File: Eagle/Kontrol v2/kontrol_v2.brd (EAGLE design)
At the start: 84.3 x 132.8 mm, 34 parts, among them K1 SRD-12VDC-SL-C

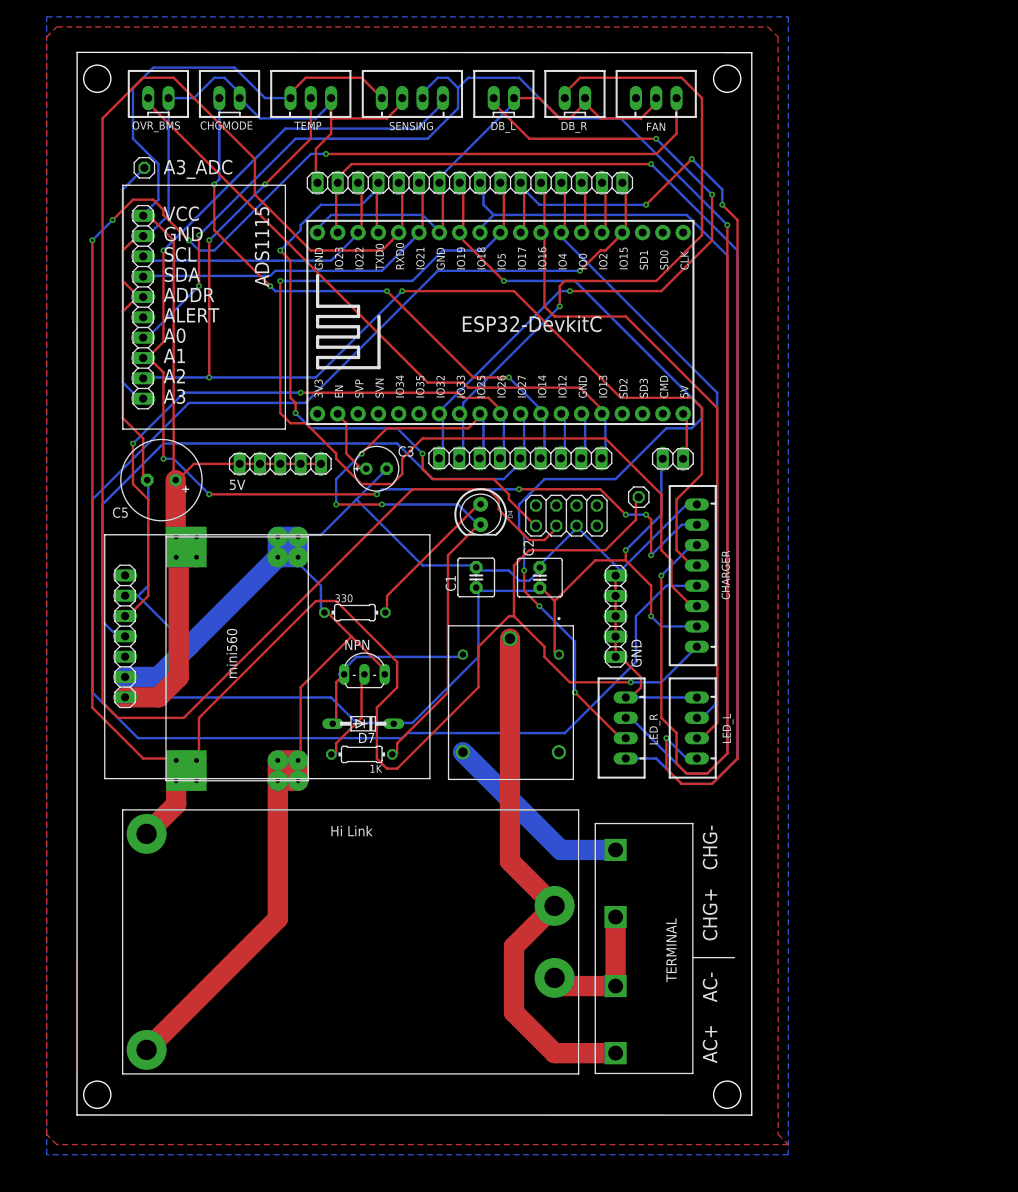
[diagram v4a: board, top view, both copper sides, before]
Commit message: Update kontrol
XH8 -> xh10
4p term -> 2p term x2
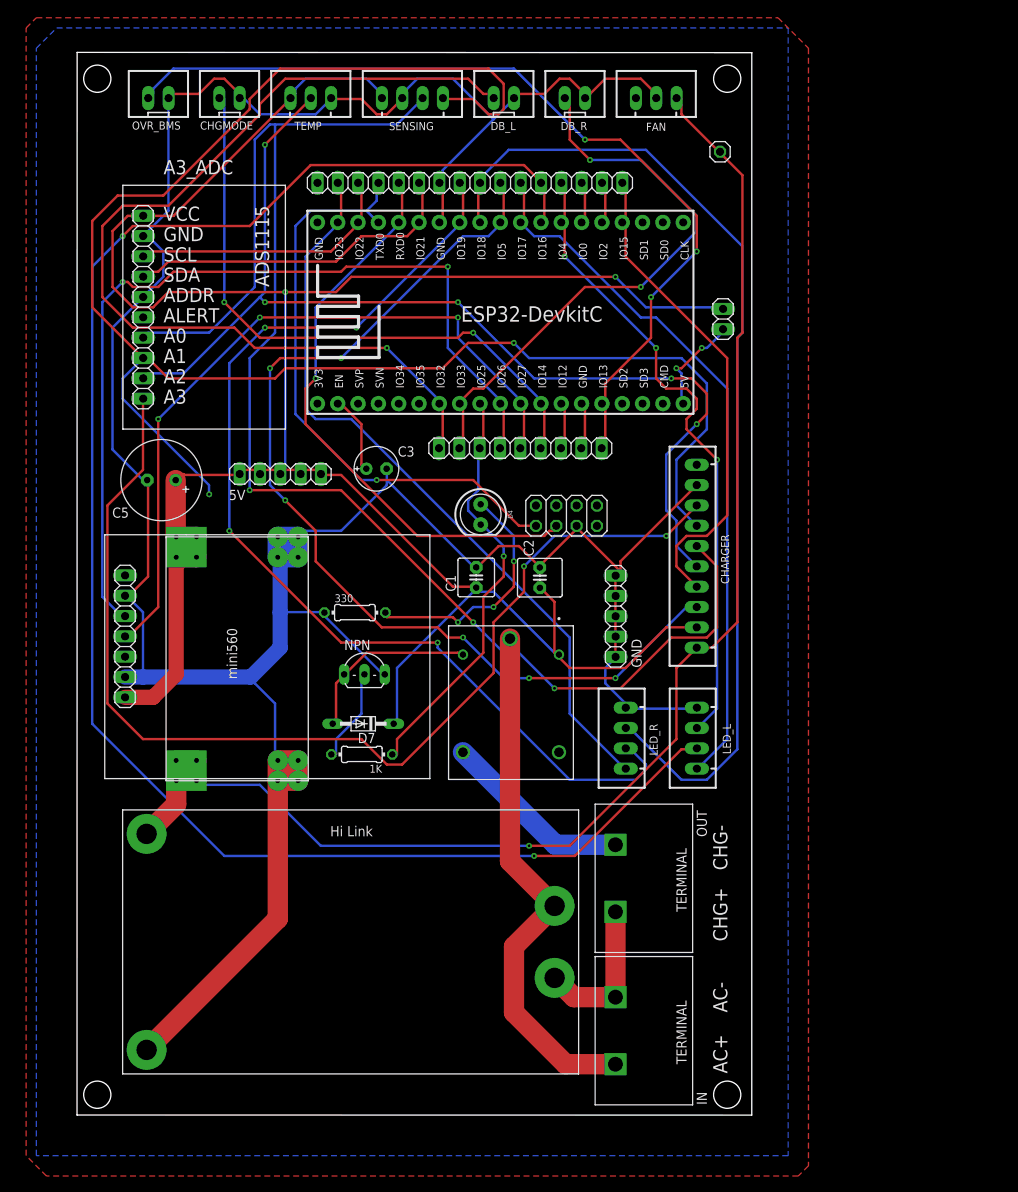
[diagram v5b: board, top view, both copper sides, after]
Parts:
- removed JP8: (no value), pinhead:1X01
- removed U$4: TERMINAL_4P, TA_library:TERMINAL_4P
- added IN, OUT: TERMINAL_2P, TA_library:TERMINAL_2P
- CHARGER: value JST-XH-08-PIN-LONG-PAD -> JST-XH-10-PIN-LONG-PAD; device Rembrandt Electronics - JST XH Connectors v1-0:JST-XH-08-PACKAGE-LONG-PAD -> Rembrandt Electronics - JST XH Connectors v1-0:JST-XH-10-PACKAGE-LONG-PAD
- moved JP4 44.4 mm to (80.4, 120.4)
- moved JP7 18.6 mm to (80.8, 99.5), turned to 270 degrees
- moved CHARGER 2.42 mm to (77.5, 69.8)
- moved U$1 1.27 mm to (52.9, 100.3)
- moved 5V 1.27 mm to (25.4, 80.1)
- moved JP6 1.27 mm to (55.4, 83.4)
- moved LED_L 1.27 mm to (77.5, 47.1)
- moved LED_R 1.27 mm to (68.6, 47.1)
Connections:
- removed net N$44: JP8.1, U$2.A3
- new net HV_SENSE: CHARGER.8, U$2.A3
- new net N$14: CHARGER.10
- net AC+: now also IN.2, OUT.1; no longer U$4.P$2, U$4.P$3
- net AC-: now also IN.1; no longer U$4.P$1
- net AC_OUT_CHG: now also OUT.2; no longer U$4.P$4
- net GND: now also CHARGER.9; no longer CHARGER.8
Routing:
- net PWM_DISCHARGE: track 200.1 -> 61.6 mm, vias 1 -> 0
- net 12V: track 315.3 -> 177.6 mm, vias 5 -> 1
- net HV_SENSE: track 0.00 -> 135.8 mm, vias 0 -> 2
- net TX_BMS: track 205.0 -> 73.3 mm, vias 0 -> 1
- net RED_KIRI: track 85.7 -> 212.9 mm, vias 0 -> 2
- net VOLTAGE_SENSE: track 148.6 -> 211.2 mm, vias 8 -> 2
- net GRN_KANAN: track 142.4 -> 94.9 mm, vias 1 -> 0
- net 5V: track 264.2 -> 307.1 mm
- net GRN_KIRI: track 129.0 -> 89.0 mm, vias 4 -> 0
- net DETEKSI_BATERAI_KIRI: track 87.7 -> 121.4 mm, vias 3 -> 1
- net OVERRIDE_BMS: track 80.2 -> 112.6 mm, vias 0 -> 3
- net RX_IOT: track 80.3 -> 112.2 mm
- net N$44: track 31.4 -> 0.00 mm
- net RELAY: track 83.4 -> 53.0 mm, vias 3 -> 1
- net RED_KANAN: track 110.2 -> 132.4 mm
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
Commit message: update kontrol
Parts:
- renumbered 330 to R2
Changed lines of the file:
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@@
 <drawing>
 <settings>
-<setting alwaysvectorfont="yes"/>
+<setting alwaysvectorfont="no"/>
 <setting verticaltext="up"/>
 </settings>
@@
 <attribute name="VALUE" x="47.074109375" y="75.04679375" size="0.6096" layer="27" font="vector" ratio="20" rot="R270" align="top-center"/>
 </element>
-<element name="330" library="rcl" library_urn="urn:adsk.eagle:library:334" package="0204/7" package3d_urn="urn:adsk.eagle:package:23498/2" value="6k" x="34.742409375" y="62.80399375" smashed="yes">
+<element name="R2" library="rcl" library_urn="urn:adsk.eagle:library:334" package="0204/7" package3d_urn="urn:adsk.eagle:package:23498/2" value="6k" x="34.742409375" y="62.80399375" smashed="yes">
 <attribute name="NAME" x="32.202409375" y="64.09939375" size="0.9906" layer="25" ratio="10"/>
 <attribute name="POPULARITY" value="48" x="34.742409375" y="62.80399375" size="1.778" layer="27" display="off"/>
@@
 <contactref element="U$3" pad="GND1"/>
 <contactref element="U$3" pad="GND"/>
-<contactref element="330" pad="1"/>
+<contactref element="R2" pad="1"/>
 <contactref element="GND" pad="1"/>
 <contactref element="GND" pad="2"/>
@@
 <signal name="N$1">
 <contactref element="D4" pad="A"/>
-<contactref element="330" pad="2"/>
+<contactref element="R2" pad="2"/>
 <wire x1="46.99" y1="62.23" x2="38.735" y2="62.23" width="0.3048" layer="1"/>
 <wire x1="47.625" y1="61.595" x2="46.99" y2="62.23" width="0.3048" layer="1"/>

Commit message: update kontrol
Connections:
- net N$1: now also D4.K; no longer D4.A
- net RELAY: now also D4.A; no longer D4.K
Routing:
- net N$1: track 30.7 -> 82.6 mm
- net RELAY: track 53.0 -> 52.0 mm
- net GND: track 396.7 -> 397.7 mm
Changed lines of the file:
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@@
 <wire x1="8.255" y1="54.75219375" x2="8.255" y2="62.865" width="0.3048" layer="16"/>
 <wire x1="6.35" y1="64.77" x2="6.015009375" y2="64.91219375" width="0.3048" layer="16"/>
-<wire x1="38.735" y1="78.74" x2="38.735" y2="79.375" width="0.3048" layer="16"/>
-<wire x1="38.735" y1="79.375" x2="38.735" y2="80.645" width="0.3048" layer="16"/>
-<wire x1="33.02" y1="73.025" x2="38.735" y2="78.74" width="0.3048" layer="16"/>
-<wire x1="28.575" y1="73.025" x2="33.02" y2="73.025" width="0.3048" layer="16"/>
+<wire x1="38.735" y1="76.2" x2="38.735" y2="78.105" width="0.3048" layer="16"/>
+<wire x1="38.735" y1="78.105" x2="38.735" y2="80.645" width="0.3048" layer="16"/>
+<wire x1="35.56" y1="73.025" x2="38.735" y2="76.2" width="0.3048" layer="16"/>
+<wire x1="28.575" y1="73.025" x2="35.56" y2="73.025" width="0.3048" layer="16"/>
 <wire x1="38.735" y1="80.645" x2="38.704809375" y2="80.78719375" width="0.3048" layer="16"/>
 <wire x1="28.575" y1="73.025" x2="27.644409375" y2="72.26419375" width="0.3048" layer="16"/>
@@
 <wire x1="25.4" y1="62.865" x2="30.48" y2="62.865" width="0.3048" layer="16"/>
 <wire x1="30.48" y1="62.865" x2="30.932409375" y2="62.80399375" width="0.3048" layer="16"/>
-<wire x1="38.735" y1="79.375" x2="49.53" y2="68.58" width="0.3048" layer="16"/>
-<wire x1="49.53" y1="68.58" x2="49.905409375" y2="68.46619375" width="0.3048" layer="16"/>
+<wire x1="38.735" y1="78.105" x2="48.37380625" y2="68.46619375" width="0.3048" layer="16"/>
+<wire x1="48.37380625" y1="68.46619375" x2="49.905409375" y2="68.46619375" width="0.3048" layer="16"/>
 <wire x1="24.765" y1="51.435" x2="24.765" y2="44.45" width="0.3048" layer="16"/>
 <wire x1="22.225" y1="53.975" x2="24.765" y2="51.435" width="0.3048" layer="16"/>
@@
 <contactref element="JP6" pad="7"/>
 <contactref element="U$1" pad="9"/>
-<contactref element="D4" pad="K"/>
 <wire x1="50.8" y1="88.9" x2="50.8" y2="83.82" width="0.3048" layer="1"/>
 <wire x1="50.8" y1="83.82" x2="50.338009375" y2="83.35259375" width="0.3048" layer="1"/>
@@
 <wire x1="53.34" y1="67.31" x2="50.8" y2="64.77" width="0.3048" layer="1"/>
 <wire x1="53.34" y1="69.85" x2="53.34" y2="67.31" width="0.3048" layer="1"/>
-<wire x1="53.34" y1="71.12" x2="53.34" y2="69.85" width="0.3048" layer="16"/>
-<wire x1="50.8" y1="73.66" x2="53.34" y2="71.12" width="0.3048" layer="16"/>
 <wire x1="40.005" y1="45.085" x2="39.416009375" y2="45.07479375" width="0.3048" layer="1"/>
-<wire x1="50.8" y1="73.66" x2="50.465009375" y2="73.80219375" width="0.3048" layer="16"/>
-<wire x1="50.165" y1="78.105" x2="50.165" y2="83.185" width="0.3048" layer="16"/>
-<wire x1="48.895" y1="76.835" x2="50.165" y2="78.105" width="0.3048" layer="16"/>
-<wire x1="48.895" y1="75.565" x2="48.895" y2="76.835" width="0.3048" layer="16"/>
-<wire x1="50.165" y1="74.295" x2="48.895" y2="75.565" width="0.3048" layer="16"/>
+<wire x1="50.165" y1="76.5175" x2="50.165" y2="83.185" width="0.3048" layer="16"/>
 <wire x1="50.165" y1="83.185" x2="50.338009375" y2="83.35259375" width="0.3048" layer="16"/>
-<wire x1="50.165" y1="74.295" x2="50.465009375" y2="73.80219375" width="0.3048" layer="16"/>
 <via x="53.34" y="69.85" extent="1-16" drill="0.35"/>
+<contactref element="D4" pad="A"/>
+<wire x1="50.165" y1="76.5175" x2="50.465009375" y2="76.34219375" width="0.3048" layer="16"/>
+<wire x1="53.34" y1="73.3425" x2="50.4825" y2="76.2" width="0.3048" layer="16"/>
+<wire x1="53.34" y1="69.85" x2="53.34" y2="73.3425" width="0.3048" layer="16"/>
+<wire x1="50.4825" y1="76.2" x2="50.465009375" y2="76.34219375" width="0.3048" layer="16"/>
 </signal>
 <signal name="AC_OUT_CHG">
@@
 <wire x1="66.04" y1="116.205" x2="65.628809375" y2="116.52499375" width="0.3048" layer="1"/>
 <wire x1="66.04" y1="111.76" x2="65.618809375" y2="111.57519375" width="0.3048" layer="1"/>
-</signal>
-<signal name="N$1">
-<contactref element="D4" pad="A"/>
-<contactref element="R2" pad="2"/>
-<wire x1="46.99" y1="62.23" x2="38.735" y2="62.23" width="0.3048" layer="1"/>
-<wire x1="47.625" y1="61.595" x2="46.99" y2="62.23" width="0.3048" layer="1"/>
-<wire x1="49.53" y1="63.5" x2="47.625" y2="61.595" width="0.3048" layer="16"/>
-<wire x1="52.07" y1="63.5" x2="49.53" y2="63.5" width="0.3048" layer="16"/>
-<wire x1="54.61" y1="66.04" x2="52.07" y2="63.5" width="0.3048" layer="1"/>
-<wire x1="54.61" y1="69.215" x2="54.61" y2="66.04" width="0.3048" layer="1"/>
-<wire x1="54.61" y1="72.39" x2="54.61" y2="69.215" width="0.3048" layer="16"/>
-<wire x1="50.8" y1="76.2" x2="54.61" y2="72.39" width="0.3048" layer="16"/>
-<wire x1="38.735" y1="62.23" x2="38.552409375" y2="62.80399375" width="0.3048" layer="1"/>
-<wire x1="50.8" y1="76.2" x2="50.465009375" y2="76.34219375" width="0.3048" layer="16"/>
-<via x="47.625" y="61.595" extent="1-16" drill="0.35"/>
-<via x="52.07" y="63.5" extent="1-16" drill="0.35"/>
-<via x="54.61" y="69.215" extent="1-16" drill="0.35"/>
 </signal>
 <signal name="TEMP_SENSE">
@@
 <contactref element="CHARGER" pad="10"/>
 </signal>
+<signal name="N$1">
+<contactref element="D4" pad="K"/>
+<contactref element="R2" pad="2"/>
+<wire x1="46.6725" y1="62.5475" x2="38.735" y2="62.5475" width="0.3048" layer="1"/>
+<wire x1="47.625" y1="61.595" x2="46.6725" y2="62.5475" width="0.3048" layer="1"/>
+<wire x1="49.53" y1="63.5" x2="47.625" y2="61.595" width="0.3048" layer="16"/>
+<wire x1="52.07" y1="63.5" x2="49.53" y2="63.5" width="0.3048" layer="16"/>
+<wire x1="52.07" y1="64.4525" x2="52.07" y2="63.5" width="0.3048" layer="1"/>
+<wire x1="54.61" y1="66.9925" x2="52.07" y2="64.4525" width="0.3048" layer="1"/>
+<wire x1="54.61" y1="69.215" x2="54.61" y2="66.9925" width="0.3048" layer="1"/>
+<wire x1="54.61" y1="75.2475" x2="54.61" y2="69.215" width="0.3048" layer="16"/>
+<wire x1="60.6425" y1="81.28" x2="54.61" y2="75.2475" width="0.3048" layer="16"/>
+<wire x1="66.04" y1="81.28" x2="60.6425" y2="81.28" width="0.3048" layer="16"/>
+<wire x1="66.9925" y1="82.2325" x2="66.04" y2="81.28" width="0.3048" layer="16"/>
+<wire x1="66.9925" y1="84.455" x2="66.9925" y2="82.2325" width="0.3048" layer="16"/>
+<wire x1="66.04" y1="85.4075" x2="66.9925" y2="84.455" width="0.3048" layer="16"/>
+<wire x1="44.7675" y1="85.4075" x2="66.04" y2="85.4075" width="0.3048" layer="16"/>
+<wire x1="43.815" y1="84.455" x2="44.7675" y2="85.4075" width="0.3048" layer="16"/>
+<wire x1="43.815" y1="80.3275" x2="43.815" y2="84.455" width="0.3048" layer="16"/>
+<wire x1="50.165" y1="73.9775" x2="43.815" y2="80.3275" width="0.3048" layer="16"/>
+<wire x1="38.735" y1="62.5475" x2="38.552409375" y2="62.80399375" width="0.3048" layer="1"/>
+<wire x1="50.165" y1="73.9775" x2="50.465009375" y2="73.80219375" width="0.3048" layer="16"/>
+<via x="47.625" y="61.595" extent="1-16" drill="0.35"/>
+<via x="52.07" y="63.5" extent="1-16" drill="0.35"/>
+<via x="54.61" y="69.215" extent="1-16" drill="0.35"/>
+</signal>
 </signals>
